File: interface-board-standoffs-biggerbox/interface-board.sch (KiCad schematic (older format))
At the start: 0 parts

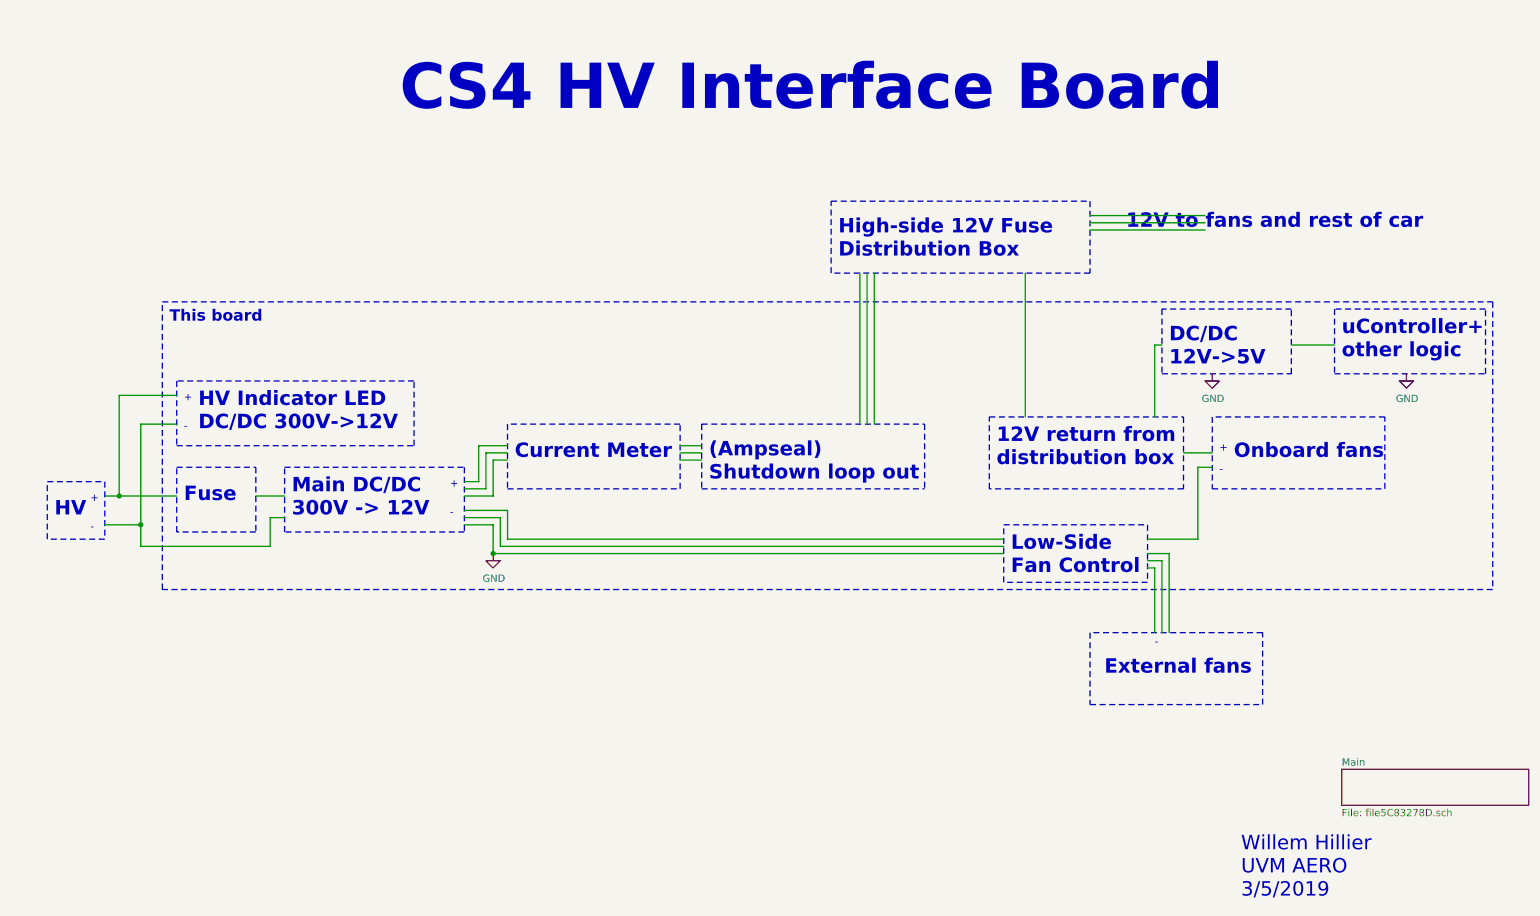
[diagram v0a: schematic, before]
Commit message: Fully working interface-board firmware, fixed wrong polarity on vicor-socket
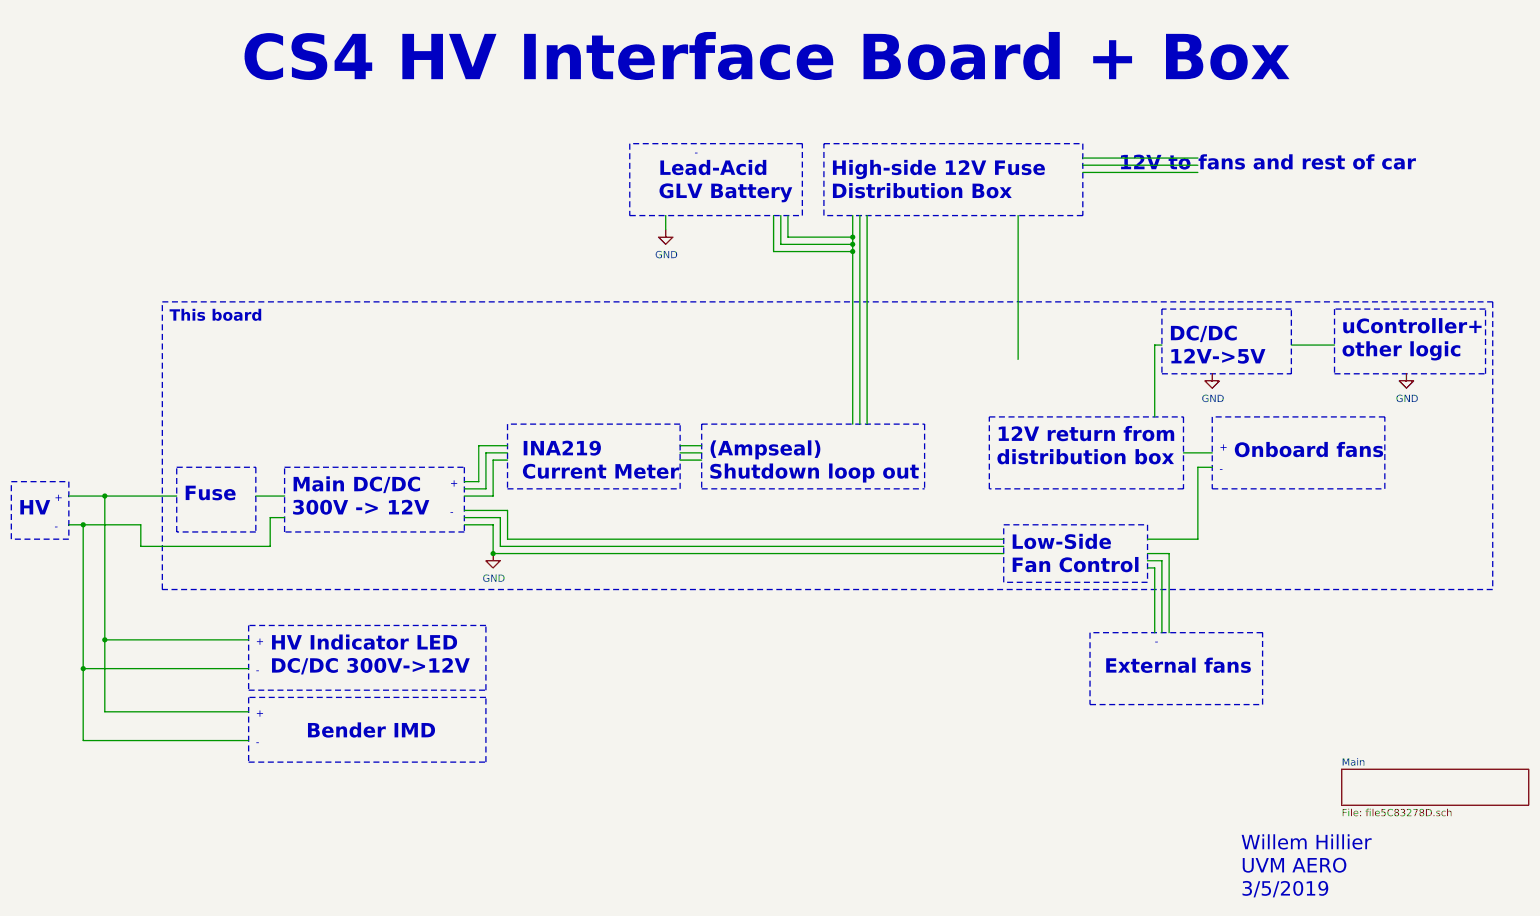
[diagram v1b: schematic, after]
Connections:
- wire segments 53 -> 68
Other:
- note added: "Bender IMD"
- note added: "CS4 HV Interface Board + Box"
- note added: "INA219\nCurrent Meter"
- note added: "Lead-Acid\nGLV Battery"
- note removed: "CS4 HV Interface Board"
- note removed: "Current Meter"
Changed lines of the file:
@@
 F1 "file5C83278D.sch" 50
 $EndSheet
-Text Notes 3250 1600 0    315  ~ 63
-CS4 HV Interface Board
-Text Notes 850  4400 0    100  ~ 20
+Text Notes 2150 1400 0    315  ~ 63
+CS4 HV Interface Board + Box
+Text Notes 600  4400 0    100  ~ 20
 HV
 Text Notes 2500 4400 0    100  ~ 20
 Main DC/DC\n300V -> 12V
-Text Notes 1850 3800 0    100  ~ 20
+Text Notes 2350 5500 0    100  ~ 20
 HV Indicator LED\nDC/DC 300V->12V
-Text Notes 4050 4000 0    100  ~ 20
-Current Meter
+Text Notes 4100 4150 0    100  ~ 20
+INA219\nCurrent Meter
 Text Notes 5400 4150 0    100  ~ 20
 (Ampseal)\nShutdown loop out
 Wire Notes Line
-	800  4150 1200 4150
-Wire Notes Line
-	1200 4150 1200 4550
-Wire Notes Line
-	1200 4550 800  4550
-Wire Notes Line
-	800  4550 800  4150
+	550  4150 950  4150
+Wire Notes Line
+	950  4150 950  4550
+Wire Notes Line
+	950  4550 550  4550
+Wire Notes Line
+	550  4550 550  4150
 Wire Notes Line
 	2450 4050 3700 4050
@@
 	5350 3750 5350 4200
 Wire Notes Line
-	1700 3450 1700 3900
-Wire Notes Line
-	1700 3900 3350 3900
-Wire Notes Line
-	3350 3900 3350 3450
-Wire Notes Line
-	3350 3450 1700 3450
+	2200 5150 2200 5600
+Wire Notes Line
+	2200 5600 3850 5600
+Wire Notes Line
+	3850 5150 2200 5150
 Text Notes 1750 4300 0    100  ~ 20
 Fuse
@@
 Wire Notes Line
 	5350 3750 6900 3750
-Text Notes 6300 2600 0    100  ~ 20
+Text Notes 6250 2200 0    100  ~ 20
 High-side 12V Fuse\nDistribution Box
 Text Notes 7400 4050 0    100  ~ 20
 12V return from\ndistribution box
 Wire Notes Line
-	8050 2200 8050 2700
-Wire Notes Line
-	8050 2700 6250 2700
-Wire Notes Line
-	6250 2700 6250 2200
-Wire Notes Line
-	6250 2200 8050 2200
+	8000 1800 8000 2300
+Wire Notes Line
+	8000 2300 6200 2300
+Wire Notes Line
+	6200 2300 6200 1800
+Wire Notes Line
+	6200 1800 8000 1800
 Wire Notes Line
 	1700 4050 2250 4050
@@
 	7350 4200 7350 3700
 Wire Wire Line
-	1200 4250 1300 4250
-Wire Wire Line
 	2250 4250 2450 4250
-Connection ~ 1300 4250
-Wire Wire Line
-	1300 4250 1700 4250
 Wire Wire Line
 	3700 4450 3900 4450
@@
 	9450 3200 9750 3200
 Wire Wire Line
-	6450 2700 6450 3750
-Wire Wire Line
-	6500 2700 6500 3750
-Wire Wire Line
-	6550 2700 6550 3750
-Wire Wire Line
-	7600 2700 7600 3700
+	6400 2300 6400 2450
+Wire Wire Line
+	7550 2300 7550 3300
 Text Notes 9050 4000 0    100  ~ 20
 Onboard fans
@@
 Wire Notes Line width 20
 	1600 4900 1600 2900
-Wire Notes Line width 20
-	1600 2900 10850 2900
 Text Notes 1650 3050 0    79   ~ 16
 This board
@@
 $EndComp
 Wire Wire Line
-	8050 2300 8850 2300
-Wire Wire Line
-	8050 2350 8850 2350
-Wire Wire Line
-	8050 2400 8850 2400
-Text Notes 8300 2400 0    100  ~ 20
+	8000 1900 8800 1900
+Wire Wire Line
+	8000 1950 8800 1950
+Wire Wire Line
+	8000 2000 8800 2000
+Text Notes 8250 2000 0    100  ~ 20
 12V to fans and rest of car
 Wire Wire Line
-	1200 4450 1450 4450
-Wire Wire Line
 	1450 4450 1450 4600
 Wire Wire Line
@@
 Wire Wire Line
 	2350 4400 2450 4400
-Text Notes 1100 4500 0    50   ~ 0
+Text Notes 850  4500 0    50   ~ 0
 -
-Text Notes 1100 4300 0    50   ~ 0
-+\n
-Wire Wire Line
-	1300 3550 1700 3550
-Wire Wire Line
-	1300 3550 1300 4250
-Wire Wire Line
-	1450 4450 1450 3750
-Wire Wire Line
-	1450 3750 1700 3750
-Connection ~ 1450 4450
-Text Notes 1750 3800 0    50   ~ 0
+Text Notes 850  4300 0    50   ~ 0
++\n
+Text Notes 2250 5500 0    50   ~ 0
 -
-Text Notes 1750 3600 0    50   ~ 0
+Text Notes 2250 5300 0    50   ~ 0
 +\n
 Text Notes 9100 7050 0    100  ~ 0
 Willem Hillier\nUVM AERO\n3/5/2019
+Wire Notes Line width 20
+	1600 2900 10850 2900
+Wire Notes Line
+	3850 5600 3850 5150
+Wire Wire Line
+	950  4250 1200 4250
+Wire Wire Line
+	950  4450 1050 4450
+Wire Wire Line
+	1050 4450 1050 5450
+Wire Wire Line
+	1050 5450 2200 5450
+Connection ~ 1050 4450
+Wire Wire Line
+	1050 4450 1450 4450
+Wire Wire Line
+	1200 4250 1200 5250
+Wire Wire Line
+	1200 5250 2200 5250
+Connection ~ 1200 4250
+Wire Wire Line
+	1200 4250 1700 4250
+Text Notes 2600 5950 0    100  ~ 20
+Bender IMD
+Wire Notes Line
+	2200 5650 2200 6100
+Wire Notes Line
+	2200 6100 3850 6100
+Wire Notes Line
+	3850 5650 2200 5650
+Text Notes 2250 6000 0    50   ~ 0
+-
+Text Notes 2250 5800 0    50   ~ 0
++\n
+Wire Notes Line
+	3850 6100 3850 5650
+Wire Wire Line
+	1050 5950 2200 5950
+Wire Wire Line
+	1200 5750 2200 5750
+Wire Wire Line
+	1050 5450 1050 5950
+Connection ~ 1050 5450
+Wire Wire Line
+	1200 5750 1200 5250
+Connection ~ 1200 5250
+Text Notes 5050 2200 0    100  ~ 20
+Lead-Acid\nGLV Battery
+Wire Notes Line
+	4850 1800 4850 2300
+Wire Notes Line
+	4850 2300 6050 2300
+Wire Notes Line
+	6050 2300 6050 1800
+Wire Notes Line
+	6050 1800 4850 1800
+Text Notes 5300 1900 0    50   ~ 0
+-\n
+Wire Wire Line
+	5950 2300 5950 2450
+Wire Wire Line
+	5950 2450 6400 2450
+Connection ~ 6400 2450
+Wire Wire Line
+	6400 2450 6400 2500
+Wire Wire Line
+	5900 2300 5900 2500
+Wire Wire Line
+	5900 2500 6400 2500
+Connection ~ 6400 2500
+Wire Wire Line
+	6400 2500 6400 2550
+Wire Wire Line
+	5850 2300 5850 2550
+Wire Wire Line
+	5850 2550 6400 2550
+Connection ~ 6400 2550
+$Comp
+L power:GND #PWR?
+U 1 1 5CB8A5EF
+P 5100 2400
+AR Path="/5C83278E/5CB8A5EF" Ref="#PWR?"  Part="1"
+AR Path="/5CB8A5EF" Ref="#PWR?"  Part="1"
+F 0 "#PWR?" H 5100 2150 50  0001 C CNN
+F 1 "GND" H 5105 2227 50  0000 C CNN
+F 2 "" H 5100 2400 50  0001 C CNN
+F 3 "" H 5100 2400 50  0001 C CNN
+	1    5100 2400
+	1    0    0    -1
+$EndComp
+Wire Wire Line
+	5100 2300 5100 2400
+Wire Wire Line
+	6400 2550 6400 3750
+Wire Wire Line
+	6450 2300 6450 3750
+Wire Wire Line
+	6500 2300 6500 3750
 $EndSCHEMATC
